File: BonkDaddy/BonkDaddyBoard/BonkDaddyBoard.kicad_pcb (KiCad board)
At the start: 2 copper layers, 70.8 x 24 mm, 28 parts, among them J1 EXP, J2 USB_B_Micro, J3 USB_A, Q3 2N7000, Q4 2N3906, SW1 Reset, U1 74AHC04

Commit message: Upgrades board to v5. Adds Bonk Daddy.
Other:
- board text added: "1.2."
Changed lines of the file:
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@@
     )
   )
+  (gr_rect (start 101.625 69.375) (end 110.9 73.4) (layer "B.SilkS") (width 0.12) (fill solid))
   (gr_line (start 50.425 59.0334) (end 50.425 64.3166) (layer "B.SilkS") (width 0.8))
   (gr_line (start 120.8 50) (end 120.8 74) (layer "Edge.Cuts") (width 0.05))
@@
   (gr_line (start 50 74) (end 120.8 74) (layer "Edge.Cuts") (width 0.05))
   (gr_line (start 50 50) (end 50 74) (layer "Edge.Cuts") (width 0.05))
-  (gr_text "Greenface Labs" (at 110.475 73.15) (layer "B.SilkS")
+  (gr_text "1.2." (at 113.25 71.4) (layer "B.SilkS")
+    (effects (font (size 1.5 1.5) (thickness 0.25)) (justify mirror))
+  )
+  (gr_text "Greenface Labs" (at 78 73.225) (layer "B.SilkS")
     (effects (font (size 0.75 0.75) (thickness 0.12)) (justify mirror))
   )
@@
     (effects (font (size 1 1) (thickness 0.15)) (justify mirror))
   )
-  (gr_text "BonkDaddy\nv 1.2" (at 80.775 55.925) (layer "B.SilkS")
+  (gr_text "BonkDaddy\nv 1.2" (at 78.475 70.25) (layer "B.SilkS")
     (effects (font (size 1.5 1.5) (thickness 0.3)) (justify mirror))
   )

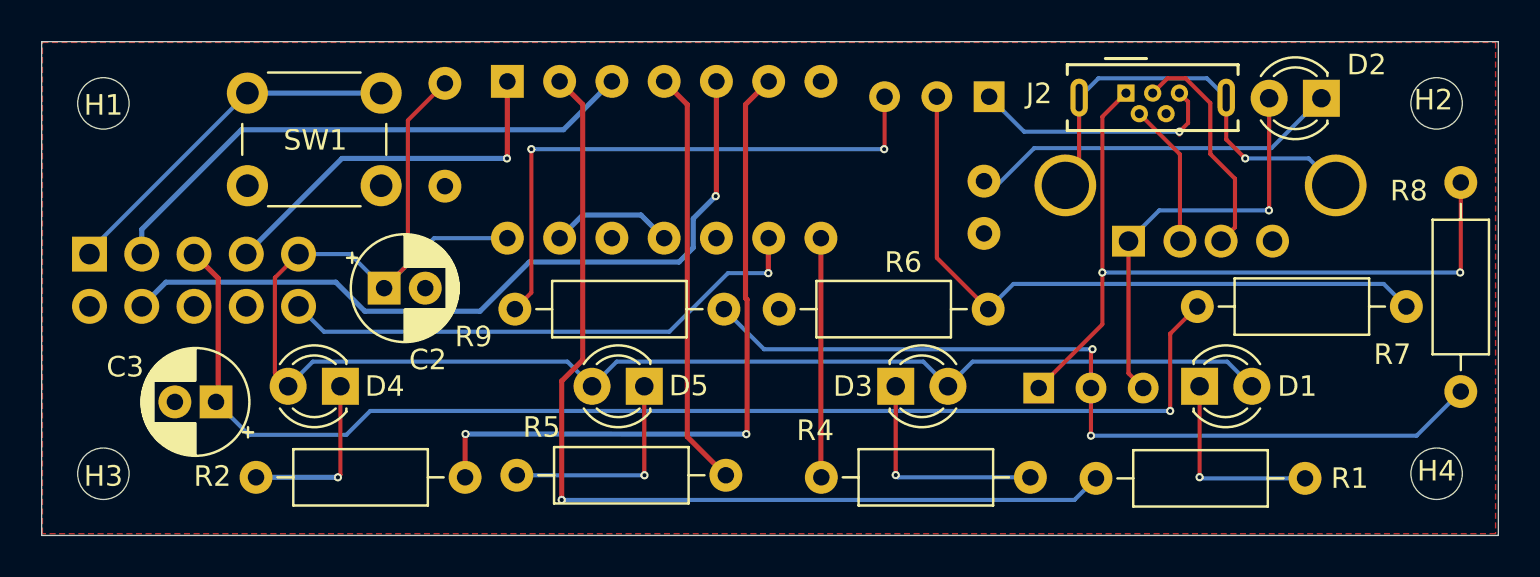
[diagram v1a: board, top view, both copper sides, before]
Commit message: Updated LED resistors
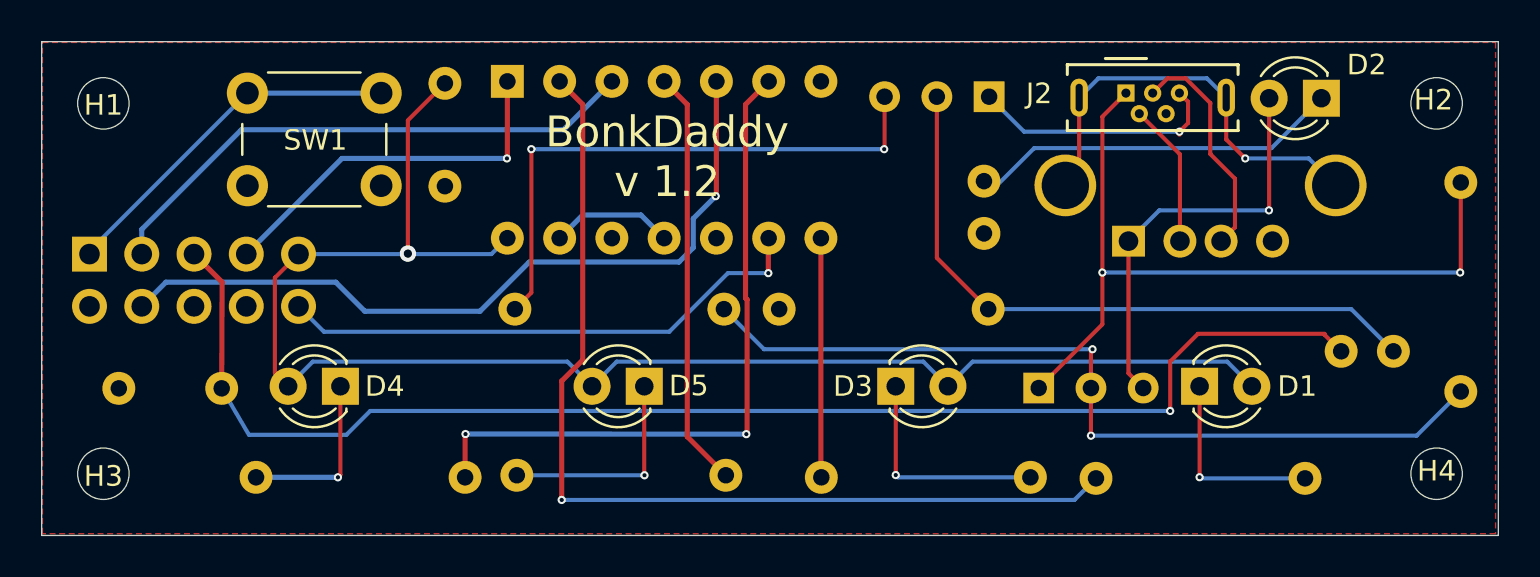
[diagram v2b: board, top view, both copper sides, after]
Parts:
- removed C2: 10uF, Capacitor_THT:CP_Radial_D5.0mm_P2.00mm
- C1: value .1uF -> 1uF
- C3: value 10uF -> 1uF; footprint Capacitor_THT:CP_Radial_D5.0mm_P2.00mm -> Capacitor_THT:C_Rect_L7.0mm_W2.0mm_P5.00mm; moved to B.Cu
- R1: value 100 -> 620; moved to B.Cu
- R2: value 75 -> 620; moved to B.Cu
- R4: value 68 -> 620; moved to B.Cu
- R5: value 47 -> 620; moved to B.Cu
- R6, R9: moved to B.Cu
- R7: value 43K -> 30K; footprint Resistor_THT:R_Axial_DIN0207_L6.3mm_D2.5mm_P10.16mm_Horizontal -> Resistor_THT:R_Axial_DIN0207_L6.3mm_D2.5mm_P2.54mm_Vertical; moved to B.Cu
- R8: value 43K -> 30K; moved to B.Cu
- U1: value 74AHC04 -> 74HC14
- moved R7 2.26 mm to (115.7, 65.0)
- moved C3 0.71 mm to (58.8, 66.8)
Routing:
- net +12V: track 60.9 -> 66.6 mm
- net +3V3: track 80.0 -> 76.5 mm, vias 0 -> 1
- net Net-(Q3-Pad2): track 32.6 -> 31.9 mm
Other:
- board text added: "10K"
- board text added: "30K"
- board text added: "620"
